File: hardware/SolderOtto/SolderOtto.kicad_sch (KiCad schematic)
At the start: 0 parts

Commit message: rework pcb
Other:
- sheet Channel0 ports: added SEL1_{a}, SEL1_{b}, SEL2_{a}, SEL2_{b}, T_{TIP}_{a}, T_{TIP}_{b}; removed DET, SEL1, SEL2, SEL3, T_{TIP}
- sheet External connection ports: added none; removed EXT_4, EXT_5
- sheet mcu ports: added Channel0_SEL1_{a}, Channel0_SEL1_{b}, Channel0_SEL2_{a}, Channel0_SEL2_{b}, Channel0_T_{TIP}_{a}, Channel0_T_{TIP}_{b}, Channel1_SEL1_{a}, Channel1_SEL1_{b}, Channel1_SEL2_{a}, Channel1_SEL2_{b}, Channel2_SEL1_{a}, Channel2_SEL1_{b}, Channel2_SEL2_{a}, Channel2_SEL2_{b}, Channel3_SEL1_{a}, Channel3_SEL1_{b}, Channel3_SEL2_{a}, Channel3_SEL2_{b}; removed Channel0_DET, Channel0_SEL1, Channel0_SEL2, Channel0_SEL3, Channel0_T_{TIP}, Channel1_DET, Channel1_SEL1, Channel1_SEL2, Channel1_SEL3, Channel2_DET, Channel2_SEL1, Channel2_SEL2, Channel2_SEL3, Channel3_DET, Channel3_SEL1, Channel3_SEL2, Channel3_SEL3, EXT_4, EXT_5

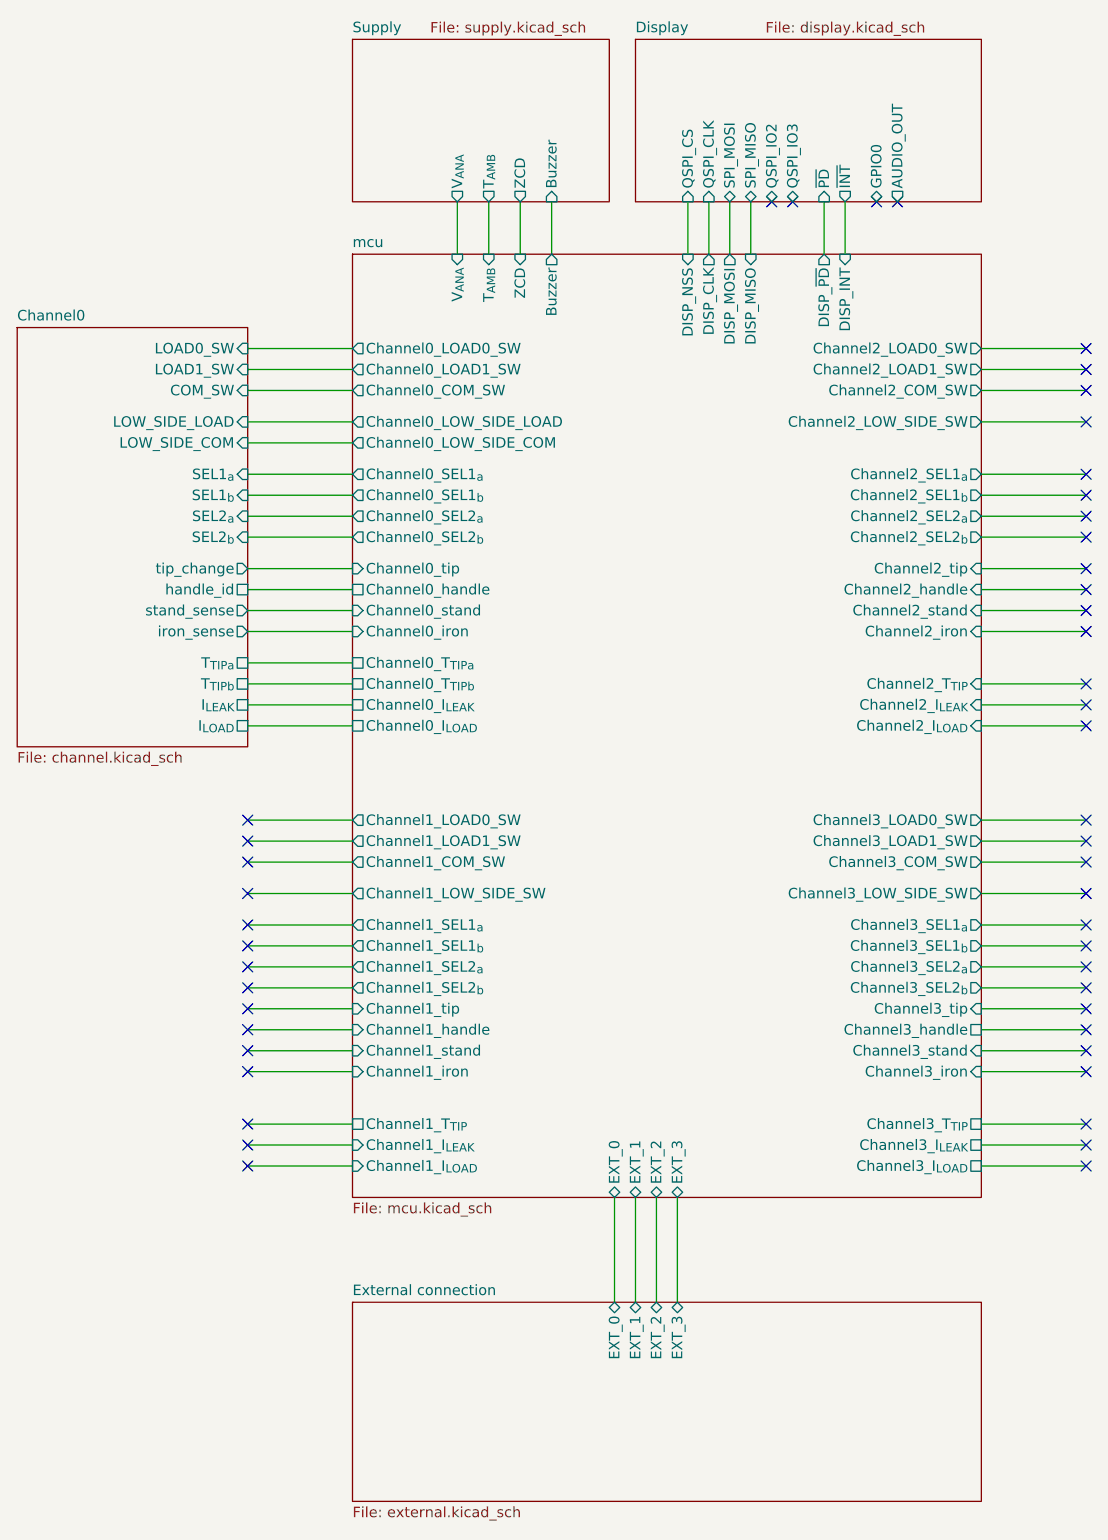
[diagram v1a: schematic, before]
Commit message: rework schematic foir single channel
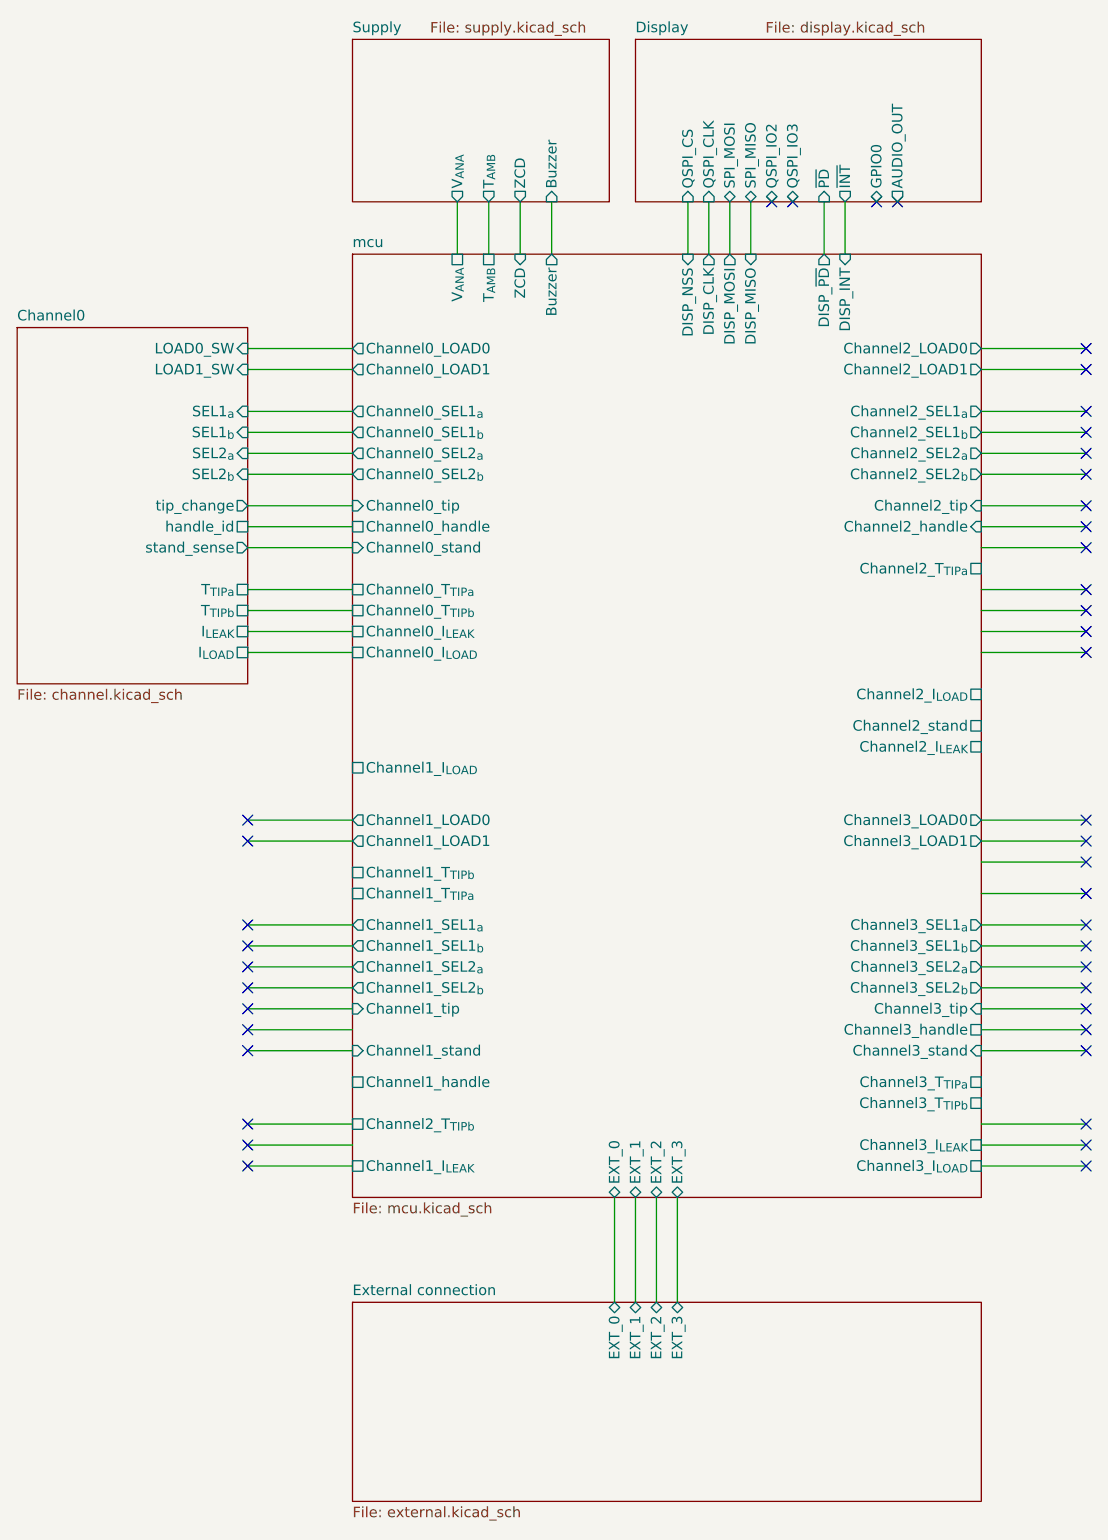
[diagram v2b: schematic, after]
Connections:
- no-connect marks 49 -> 43
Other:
- sheet Channel0 ports: added none; removed COM_SW, LOW_SIDE_COM, LOW_SIDE_LOAD, iron_sense
- sheet mcu ports: added Channel0_LOAD0, Channel0_LOAD1, Channel1_LOAD0, Channel1_LOAD1, Channel1_T_{TIP}_{a}, Channel1_T_{TIP}_{b}, Channel2_LOAD0, Channel2_LOAD1, Channel2_T_{TIP}_{a}, Channel2_T_{TIP}_{b}, Channel3_LOAD0, Channel3_LOAD1, Channel3_T_{TIP}_{a}, Channel3_T_{TIP}_{b}; removed Channel0_COM_SW, Channel0_LOAD0_SW, Channel0_LOAD1_SW, Channel0_LOW_SIDE_COM, Channel0_LOW_SIDE_LOAD, Channel0_iron, Channel1_COM_SW, Channel1_LOAD0_SW, Channel1_LOAD1_SW, Channel1_LOW_SIDE_SW, Channel1_T_{TIP}, Channel1_iron, Channel2_COM_SW, Channel2_LOAD0_SW, Channel2_LOAD1_SW, Channel2_LOW_SIDE_SW, Channel2_T_{TIP}, Channel2_iron, Channel3_COM_SW, Channel3_LOAD0_SW, Channel3_LOAD1_SW, Channel3_LOW_SIDE_SW, Channel3_T_{TIP}, Channel3_iron

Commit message: save shit
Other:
- sheet Channel0 ports: added DET; removed none
- sheet mcu ports: added Channel0_det; removed none
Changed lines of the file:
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@@
+	(wire
+		(pts
+			(xy 76.2 90.17) (xy 88.9 90.17)
+		)
+		(stroke
+			(width 0)
+			(type default)
+		)
+	)
+	(wire
+		(pts
+			(xy 134.62 38.1) (xy 134.62 44.45)
+		)
+		(stroke
+			(width 0)
+			(type default)
+		)
+	)
+	(wire
+		(pts
+			(xy 129.54 38.1) (xy 129.54 44.45)
+		)
+		(stroke
+			(width 0)
+			(type default)
+		)
+	)
+	(wire
+		(pts
+			(xy 165.1 80.01) (xy 177.8 80.01)
+		)
+		(stroke
+			(width 0)
+			(type default)
+		)
+	)
+	(wire
+		(pts
+			(xy 109.22 38.1) (xy 109.22 44.45)
+		)
+		(stroke
+			(width 0)
+			(type default)
+		)
+	)
+	(wire
+		(pts
+			(xy 165.1 125.73) (xy 177.8 125.73)
+		)
+		(stroke
+			(width 0)
+			(type default)
+		)
+	)
+	(wire
+		(pts
+			(xy 165.1 92.71) (xy 177.8 92.71)
+		)
+		(stroke
+			(width 0)
+			(type default)
+		)
+	)
+	(wire
+		(pts
+			(xy 165.1 128.27) (xy 177.8 128.27)
+		)
+		(stroke
+			(width 0)
+			(type default)
+		)
+	)
+	(wire
+		(pts
+			(xy 76.2 154.94) (xy 88.9 154.94)
+		)
+		(stroke
+			(width 0)
+			(type default)
+		)
+	)
+	(wire
+		(pts
+			(xy 165.1 135.89) (xy 177.8 135.89)
+		)
+		(stroke
+			(width 0)
+			(type default)
+		)
+	)
+	(wire
+		(pts
+			(xy 120.65 158.75) (xy 120.65 171.45)
+		)
+		(stroke
+			(width 0)
+			(type default)
+		)
+	)
+	(wire
+		(pts
+			(xy 165.1 71.12) (xy 177.8 71.12)
+		)
+		(stroke
+			(width 0)
+			(type default)
+		)
+	)
+	(wire
+		(pts
+			(xy 76.2 140.97) (xy 88.9 140.97)
+		)
+		(stroke
+			(width 0)
+			(type default)
+		)
+	)
+	(wire
+		(pts
+			(xy 101.6 38.1) (xy 101.6 44.45)
+		)
+		(stroke
+			(width 0)
+			(type default)
+		)
+	)
+	(wire
+		(pts
+			(xy 165.1 74.93) (xy 177.8 74.93)
+		)
+		(stroke
+			(width 0)
+			(type default)
+		)
+	)
+	(wire
+		(pts
+			(xy 76.2 63.5) (xy 88.9 63.5)
+		)
+		(stroke
+			(width 0)
+			(type default)
+		)
+	)
+	(wire
+		(pts
+			(xy 76.2 135.89) (xy 88.9 135.89)
+		)
+		(stroke
+			(width 0)
+			(type default)
+		)
+	)
+	(wire
+		(pts
+			(xy 76.2 149.86) (xy 88.9 149.86)
+		)
+		(stroke
+			(width 0)
+			(type default)
+		)
+	)
+	(wire
+		(pts
+			(xy 165.1 77.47) (xy 177.8 77.47)
+		)
+		(stroke
+			(width 0)
+			(type default)
+		)
+	)
 	(wire
 		(pts
@@
 	(wire
 		(pts
-			(xy 134.62 38.1) (xy 134.62 44.45)
-		)
-		(stroke
-			(width 0)
-			(type default)
-		)
-	)
-	(wire
-		(pts
-			(xy 129.54 38.1) (xy 129.54 44.45)
-		)
-		(stroke
-			(width 0)
-			(type default)
-		)
-	)
-	(wire
-		(pts
-			(xy 165.1 80.01) (xy 177.8 80.01)
-		)
-		(stroke
-			(width 0)
-			(type default)
-		)
-	)
-	(wire
-		(pts
-			(xy 109.22 38.1) (xy 109.22 44.45)
-		)
-		(stroke
-			(width 0)
-			(type default)
-		)
-	)
-	(wire
-		(pts
-			(xy 165.1 125.73) (xy 177.8 125.73)
-		)
-		(stroke
-			(width 0)
-			(type default)
-		)
-	)
-	(wire
-		(pts
-			(xy 165.1 92.71) (xy 177.8 92.71)
-		)
-		(stroke
-			(width 0)
-			(type default)
-		)
-	)
-	(wire
-		(pts
-			(xy 165.1 128.27) (xy 177.8 128.27)
-		)
-		(stroke
-			(width 0)
-			(type default)
-		)
-	)
-	(wire
-		(pts
-			(xy 76.2 154.94) (xy 88.9 154.94)
-		)
-		(stroke
-			(width 0)
-			(type default)
-		)
-	)
-	(wire
-		(pts
-			(xy 165.1 135.89) (xy 177.8 135.89)
-		)
-		(stroke
-			(width 0)
-			(type default)
-		)
-	)
-	(wire
-		(pts
-			(xy 120.65 158.75) (xy 120.65 171.45)
-		)
-		(stroke
-			(width 0)
-			(type default)
-		)
-	)
-	(wire
-		(pts
-			(xy 165.1 71.12) (xy 177.8 71.12)
-		)
-		(stroke
-			(width 0)
-			(type default)
-		)
-	)
-	(wire
-		(pts
-			(xy 76.2 140.97) (xy 88.9 140.97)
-		)
-		(stroke
-			(width 0)
-			(type default)
-		)
-	)
-	(wire
-		(pts
-			(xy 101.6 38.1) (xy 101.6 44.45)
-		)
-		(stroke
-			(width 0)
-			(type default)
-		)
-	)
-	(wire
-		(pts
-			(xy 165.1 74.93) (xy 177.8 74.93)
-		)
-		(stroke
-			(width 0)
-			(type default)
-		)
-	)
-	(wire
-		(pts
-			(xy 76.2 63.5) (xy 88.9 63.5)
-		)
-		(stroke
-			(width 0)
-			(type default)
-		)
-	)
-	(wire
-		(pts
-			(xy 76.2 135.89) (xy 88.9 135.89)
-		)
-		(stroke
-			(width 0)
-			(type default)
-		)
-	)
-	(wire
-		(pts
-			(xy 76.2 149.86) (xy 88.9 149.86)
-		)
-		(stroke
-			(width 0)
-			(type default)
-		)
-	)
-	(wire
-		(pts
-			(xy 165.1 77.47) (xy 177.8 77.47)
-		)
-		(stroke
-			(width 0)
-			(type default)
-		)
-	)
-	(wire
-		(pts
-			(xy 76.2 85.09) (xy 88.9 85.09)
-		)
-		(stroke
-			(width 0)
-			(type default)
-		)
-	)
-	(wire
-		(pts
 			(xy 76.2 77.47) (xy 88.9 77.47)
 		)
@@
 	(wire
 		(pts
-			(xy 76.2 90.17) (xy 88.9 90.17)
+			(xy 76.2 92.71) (xy 88.9 92.71)
 		)
 		(stroke
@@
 	(wire
 		(pts
+			(xy 76.2 82.55) (xy 88.9 82.55)
+		)
+		(stroke
+			(width 0)
+			(type default)
+		)
+	)
+	(wire
+		(pts
 			(xy 76.2 130.81) (xy 88.9 130.81)
 		)
@@
 	(wire
 		(pts
-			(xy 76.2 92.71) (xy 88.9 92.71)
+			(xy 76.2 95.25) (xy 88.9 95.25)
 		)
 		(stroke
@@
 	(sheet
 		(at 48.26 53.34)
-		(size 27.94 43.18)
+		(size 27.94 45.72)
 		(exclude_from_sim no)
 		(in_bom yes)
@@
 		)
 		(property "Sheetfile" "channel.kicad_sch"
-			(at 48.26 97.1046 0)
+			(at 48.26 99.6446 0)
 			(effects
 				(font
@@
 		)
 		(pin "I_{LEAK}" passive
-			(at 76.2 90.17 0)
+			(at 76.2 92.71 0)
 			(effects
 				(font
@@
 		)
 		(pin "I_{LOAD}" passive
-			(at 76.2 92.71 0)
+			(at 76.2 95.25 0)
 			(effects
 				(font
@@
 		)
 		(pin "T_{TIP}_{a}" passive
-			(at 76.2 85.09 0)
+			(at 76.2 87.63 0)
 			(effects
 				(font
@@
 		)
 		(pin "T_{TIP}_{b}" passive
-			(at 76.2 87.63 0)
+			(at 76.2 90.17 0)
+			(effects
+				(font
+					(size 1.27 1.27)
+				)
+				(justify right)
+			)
+		)
+		(pin "DET" output
+			(at 76.2 82.55 0)
 			(effects
 				(font
@@
 		)
 		(pin "Channel0_I_{LEAK}" passive
-			(at 88.9 90.17 180)
+			(at 88.9 92.71 180)
 			(effects
 				(font
@@
 		)
 		(pin "Channel0_I_{LOAD}" passive
-			(at 88.9 92.71 180)
+			(at 88.9 95.25 180)
 			(effects
 				(font
@@
 		)
 		(pin "Channel0_T_{TIP}_{b}" passive
+			(at 88.9 90.17 180)
+			(effects
+				(font
+					(size 1.27 1.27)
+				)
+				(justify left)
+			)
+		)
+		(pin "Channel0_T_{TIP}_{a}" passive
 			(at 88.9 87.63 180)
-			(effects
-				(font
-					(size 1.27 1.27)
-				)
-				(justify left)
-			)
-		)
-		(pin "Channel0_T_{TIP}_{a}" passive
-			(at 88.9 85.09 180)
 			(effects
 				(font
@@
 			)
 		)
+		(pin "Channel0_det" input
+			(at 88.9 82.55 180)
+			(effects
+				(font
+					(size 1.27 1.27)
+				)
+				(justify left)
+			)
+		)
